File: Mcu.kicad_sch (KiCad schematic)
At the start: 11 parts, among them J2 USB C 2.0 16P, M1 Module-mega-mcu144-0.7, P23 BOOT0, P24 SWDIO, P25 SWCLK, P26 NRST, U1 USBLC6-2SC6

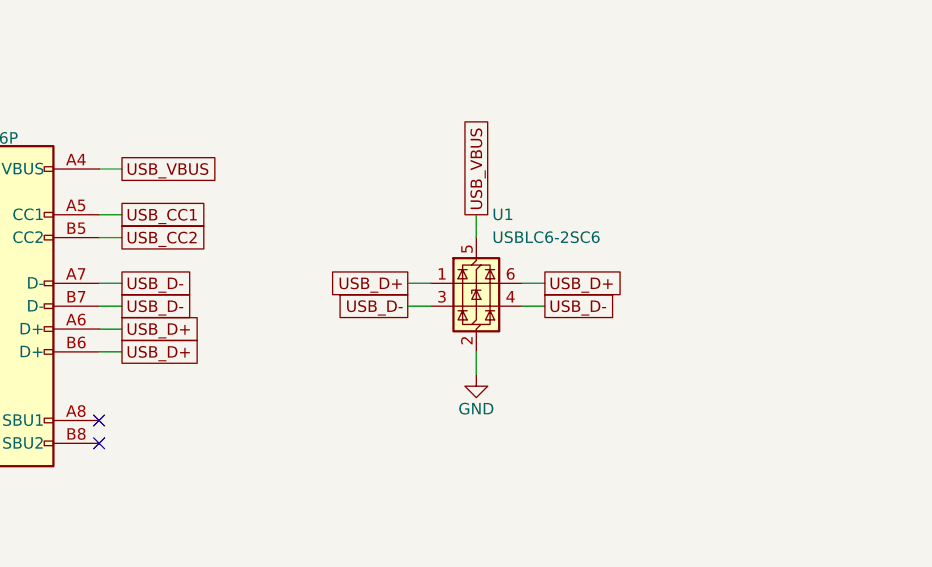
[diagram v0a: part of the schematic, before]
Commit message: U1 is the library USBLC6-2SC6 (EE-C-0146); J2 part numbers; test pads and proto area out of the BOM
- U1 used the USBLC6-2P6 (SOT-666) symbol with a hand-changed footprint; now EmbeddedEra:USBLC6-2SC6.
- J2 instance had no Manufacturer/MPN although the library has them.
- P1-P32 and G1 are pads, nothing is bought (SOP-008 step 18): in_bom no, as in the library.

Co-Authored-By: Claude Opus 5.5 <noreply@anthropic.com>
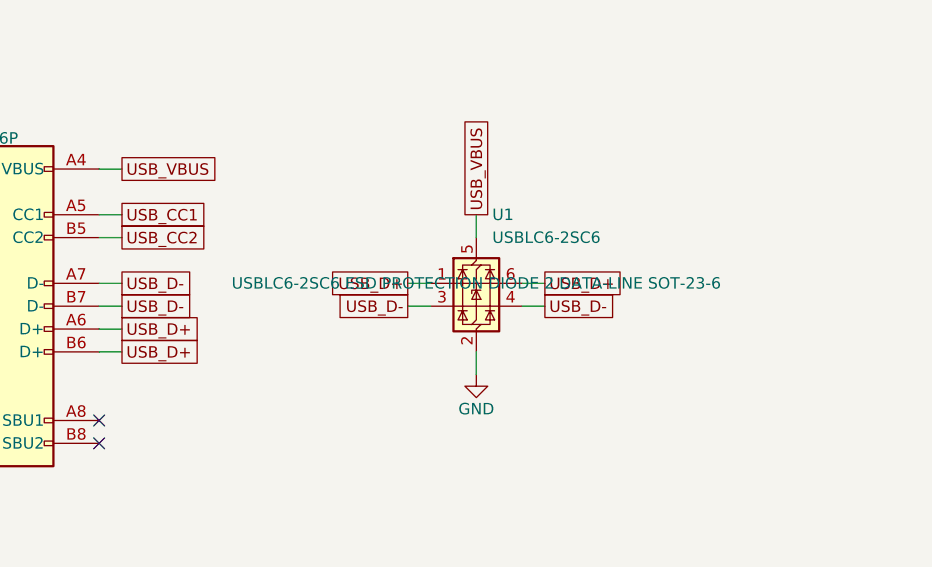
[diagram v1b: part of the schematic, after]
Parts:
- P23, P24, P25, P26: now left out of the parts list
- U1: symbol EmbeddedEra:USBLC6-2P6 -> EmbeddedEra:USBLC6-2SC6
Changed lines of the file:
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@@
 		(body_style 1)
 		(exclude_from_sim no)
-		(in_bom yes)
+		(in_bom no)
 		(on_board yes)
 		(in_pos_files yes)
@@
 		(body_style 1)
 		(exclude_from_sim no)
-		(in_bom yes)
+		(in_bom no)
 		(on_board yes)
 		(in_pos_files yes)
@@
 		(body_style 1)
 		(exclude_from_sim no)
-		(in_bom yes)
+		(in_bom no)
 		(on_board yes)
 		(in_pos_files yes)
@@
 		(body_style 1)
 		(exclude_from_sim no)
-		(in_bom yes)
+		(in_bom no)
 		(on_board yes)
 		(in_pos_files yes)
@@
 	)
 	(symbol
-		(lib_id "EmbeddedEra:USBLC6-2P6")
+		(lib_id "EmbeddedEra:USBLC6-2SC6")
 		(at 220.98 60.96 0)
 		(unit 1)
@@
 			)
 		)
-		(property "Datasheet" ""
+		(property "Datasheet" "https://www.st.com/resource/en/datasheet/usblc6-2.pdf"
 			(at 220.98 60.96 0)
 			(hide yes)
@@
 			)
 		)
-		(property "Description" ""
+		(property "Description" "USBLC6-2SC6 ESD PROTECTION DIODE 2 DATA-LINE SOT-23-6"
 			(at 220.98 60.96 0)
 			(show_name no)

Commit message: Title block: TITLE is the project name (${Project_Name}) on every sheet, DESCRIPTION the sheet name
The LS/INJ sub-sheet and the root had no title at all.

Co-Authored-By: Claude Opus 5.5 <noreply@anthropic.com>
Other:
- title: MCU and USB -> ${Project_Name}
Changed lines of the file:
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@@
 	(paper "A3" portrait)
 	(title_block
-		(title "MCU and USB")
+		(title "${Project_Name}")
 		(date "2026-10-13")
 	)

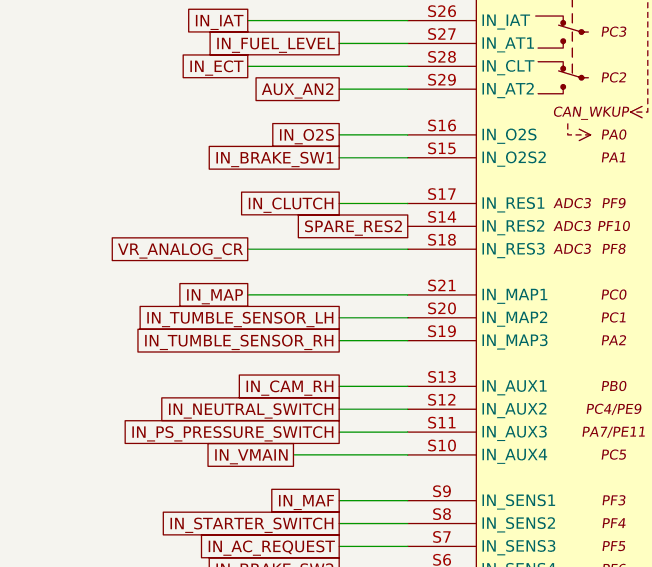
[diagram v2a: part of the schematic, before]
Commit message: On-board MAP sensor (AlphaX style): U20 MPXHZ6400AC6T1 + C1 100n on +5VA -> M1 IN_MAP3 (S19)
TGV position RH moves from IN_MAP3 to IN_RES2 (S14). J3 pin 8 (was AUX_AN1 on
IN_RES2) is now not connected; P28 is the MAP test pad. External MAP stays on
IN_MAP1. PCB: U20/C1 placed left of M1, DRC 0 errors, unconnected 322.

Co-Authored-By: Claude Opus 5.5 <noreply@anthropic.com>
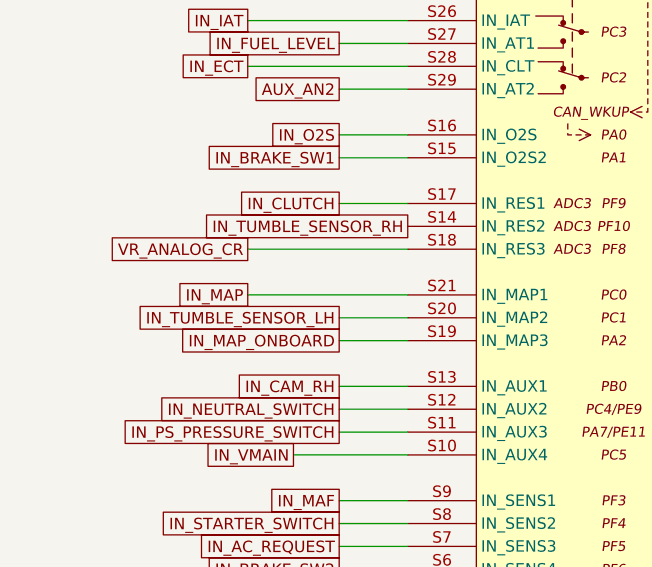
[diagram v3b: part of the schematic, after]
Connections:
- net SPARE_RES2 is gone; now on net IN_TUMBLE_SENSOR_RH: M1.S14 (IN_RES2)
- net IN_TUMBLE_SENSOR_RH: no longer M1.S19 (IN_MAP3)
- new net IN_MAP_ONBOARD: M1.S19 (IN_MAP3)

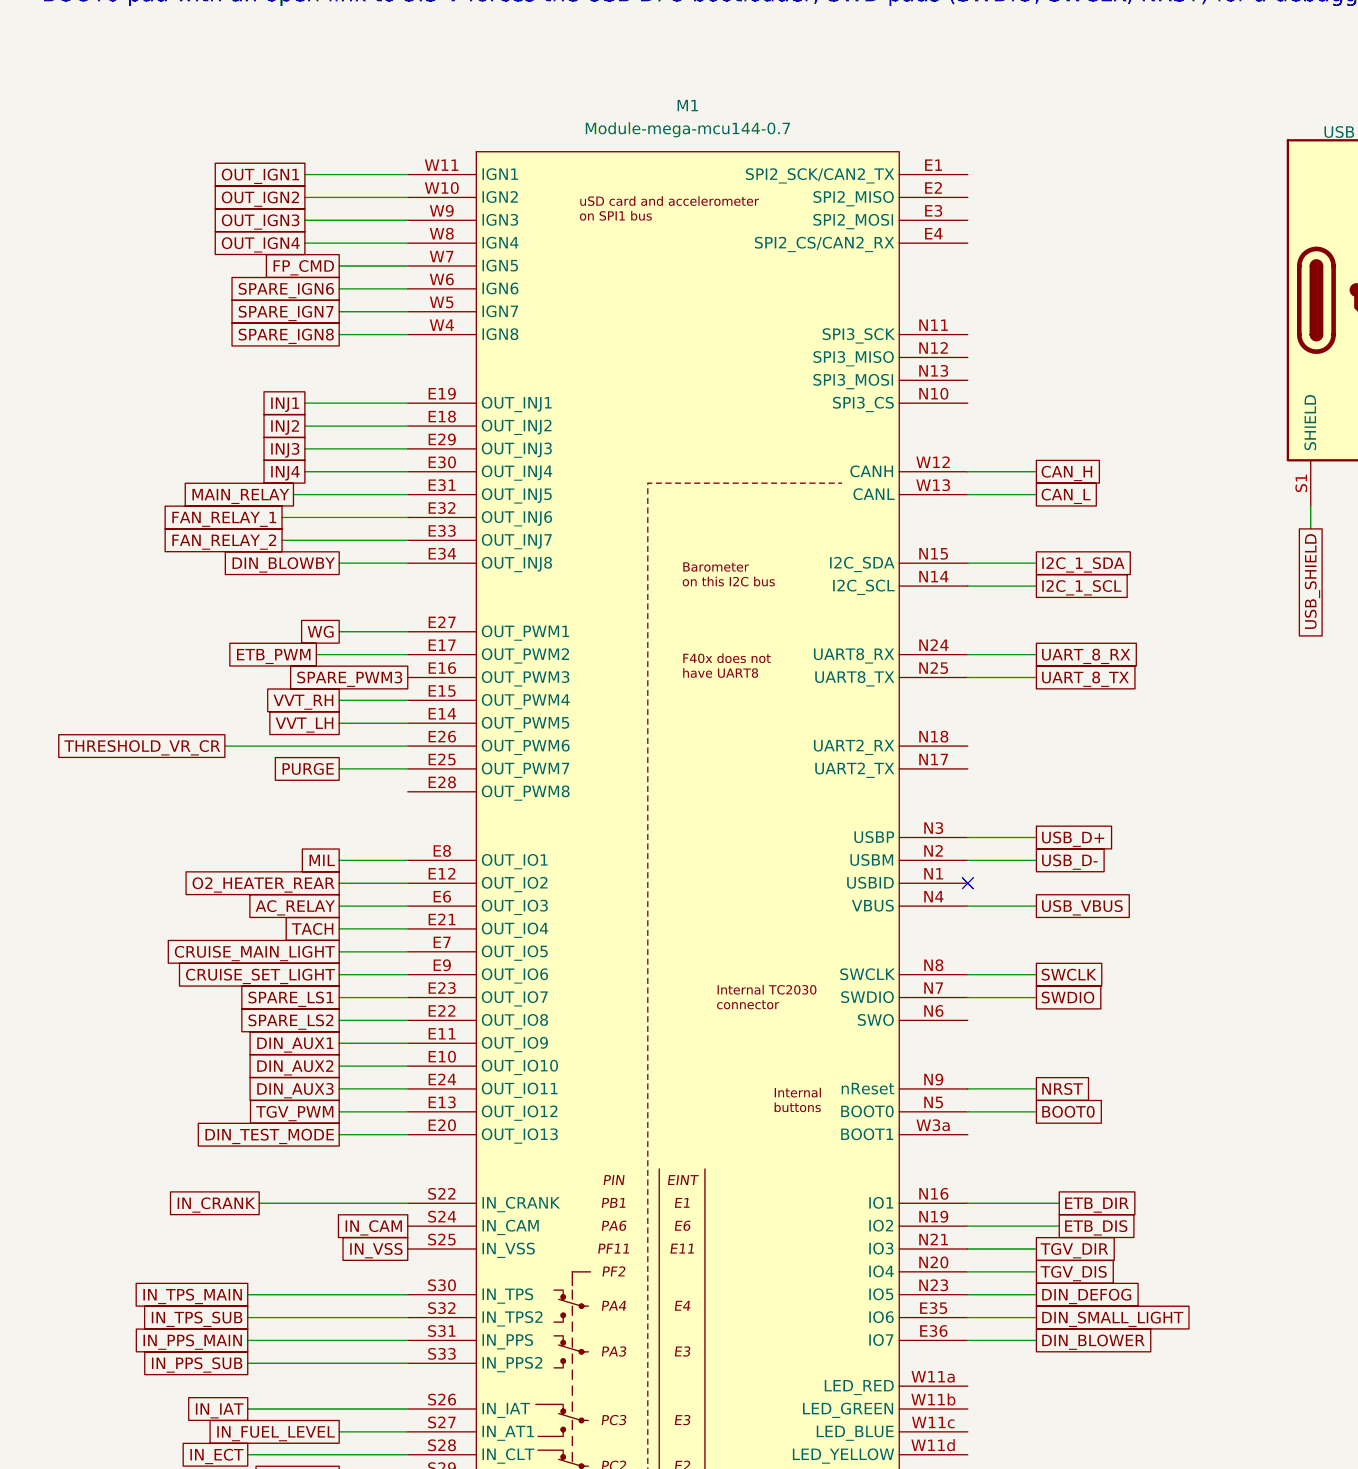
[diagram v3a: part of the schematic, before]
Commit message: M1 pin swap within module pin families (owner-approved); moved nets' copper ripped for re-routing
Co-Authored-By: Claude Opus 5.5 <noreply@anthropic.com>
Claude-Session: https://claude.ai/code/session_01Wvm7Ln3a66CJUfUkcDdYMo
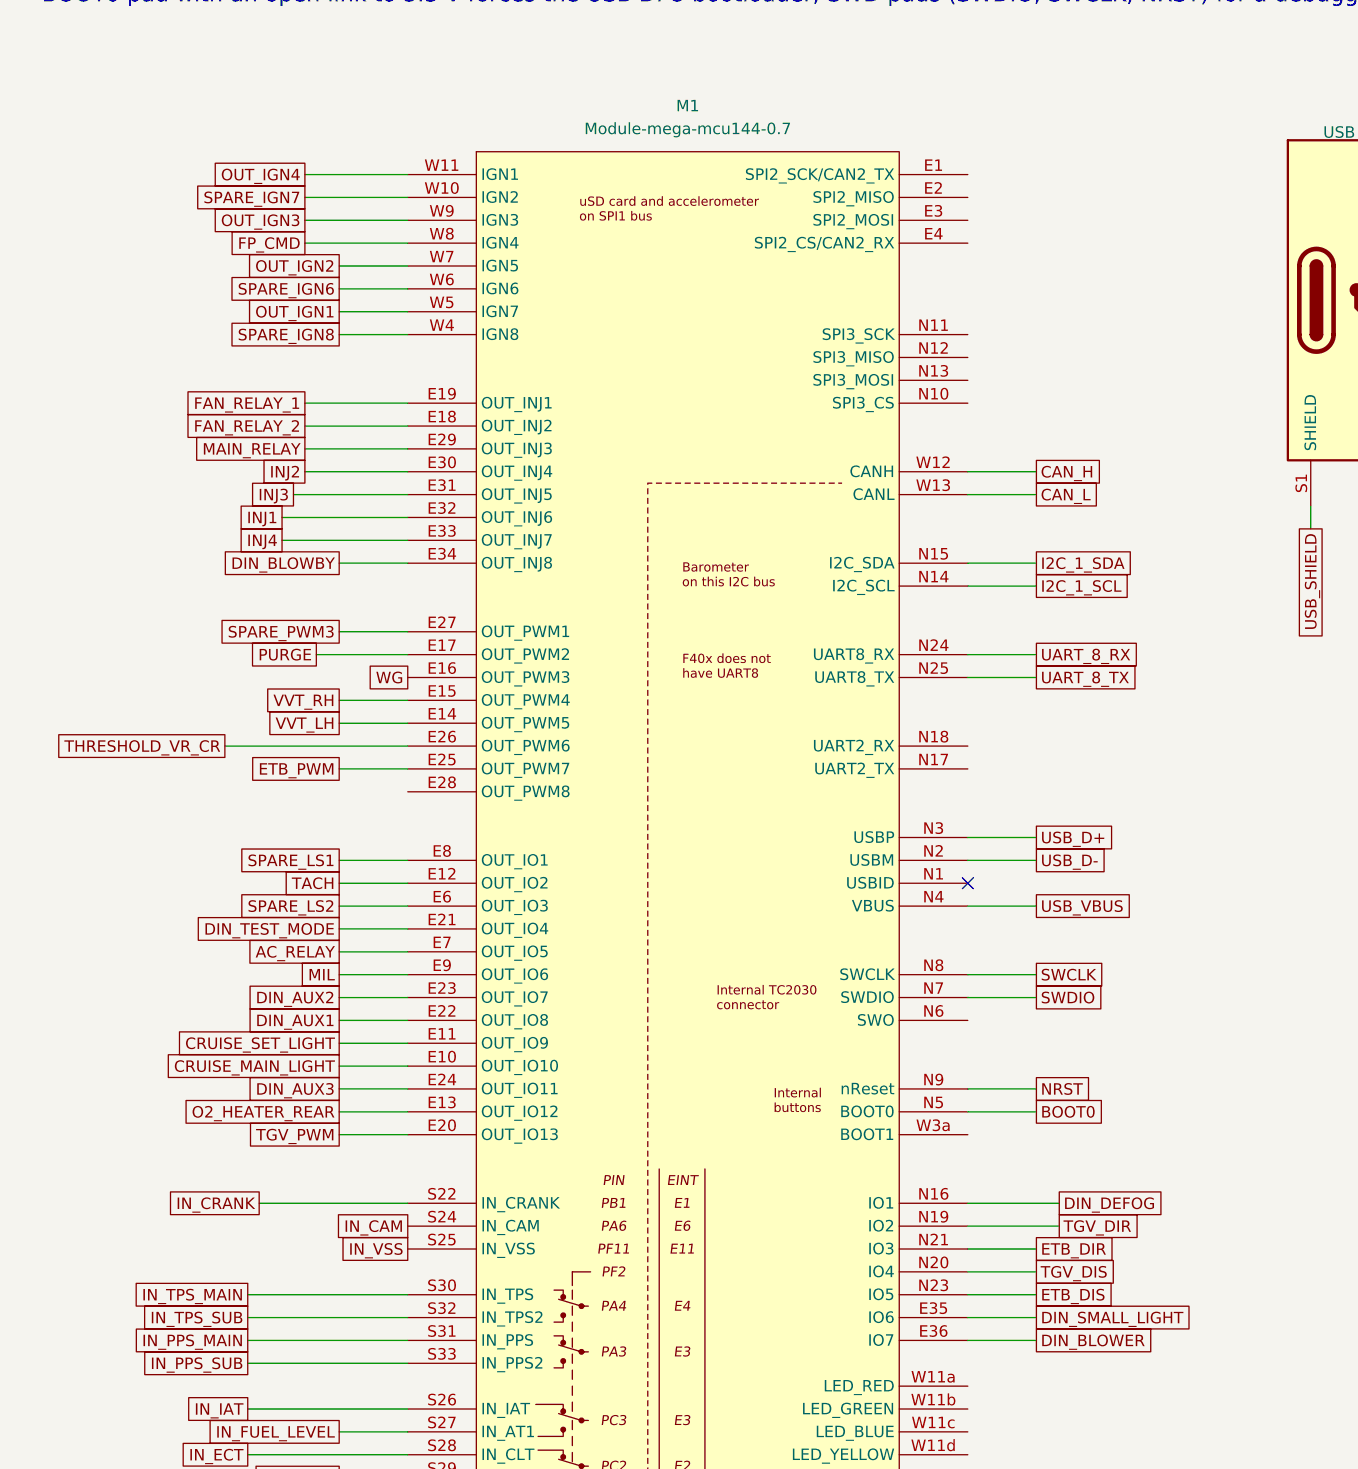
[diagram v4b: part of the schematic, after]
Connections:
- net AC_RELAY: now also M1.E7 (OUT_IO5); no longer M1.E6 (OUT_IO3)
- net CRUISE_MAIN_LIGHT: now also M1.E10 (OUT_IO10); no longer M1.E7 (OUT_IO5)
- net CRUISE_SET_LIGHT: now also M1.E11 (OUT_IO9); no longer M1.E9 (OUT_IO6)
- net DIN_AUX1: now also M1.E22 (OUT_IO8); no longer M1.E11 (OUT_IO9)
- net DIN_AUX2: now also M1.E23 (OUT_IO7); no longer M1.E10 (OUT_IO10)
- net DIN_DEFOG: now also M1.N16 (IO1); no longer M1.N23 (IO5)
- net DIN_TEST_MODE: now also M1.E21 (OUT_IO4); no longer M1.E20 (OUT_IO13)
- net ETB_DIR: now also M1.N21 (IO3); no longer M1.N16 (IO1)
- net ETB_DIS: now also M1.N23 (IO5); no longer M1.N19 (IO2)
- net ETB_PWM: now also M1.E25 (OUT_PWM7); no longer M1.E17 (OUT_PWM2)
- net FAN_RELAY_1: now also M1.E19 (OUT_INJ1); no longer M1.E32 (OUT_INJ6)
- net FAN_RELAY_2: now also M1.E18 (OUT_INJ2); no longer M1.E33 (OUT_INJ7)
- net FP_CMD: now also M1.W8 (IGN4); no longer M1.W7 (IGN5)
- net INJ1: now also M1.E32 (OUT_INJ6); no longer M1.E19 (OUT_INJ1)
- net INJ2: now also M1.E30 (OUT_INJ4); no longer M1.E18 (OUT_INJ2)
- net INJ3: now also M1.E31 (OUT_INJ5); no longer M1.E29 (OUT_INJ3)
- net INJ4: now also M1.E33 (OUT_INJ7); no longer M1.E30 (OUT_INJ4)
- net MAIN_RELAY: now also M1.E29 (OUT_INJ3); no longer M1.E31 (OUT_INJ5)
- net MIL: now also M1.E9 (OUT_IO6); no longer M1.E8 (OUT_IO1)
- net O2_HEATER_REAR: now also M1.E13 (OUT_IO12); no longer M1.E12 (OUT_IO2)
- net OUT_IGN1: now also M1.W5 (IGN7); no longer M1.W11 (IGN1)
- net OUT_IGN2: now also M1.W7 (IGN5); no longer M1.W10 (IGN2)
- net OUT_IGN4: now also M1.W11 (IGN1); no longer M1.W8 (IGN4)
- net PURGE: now also M1.E17 (OUT_PWM2); no longer M1.E25 (OUT_PWM7)
- net SPARE_IGN7: now also M1.W10 (IGN2); no longer M1.W5 (IGN7)
- net SPARE_LS1: now also M1.E8 (OUT_IO1); no longer M1.E23 (OUT_IO7)
- net SPARE_LS2: now also M1.E6 (OUT_IO3); no longer M1.E22 (OUT_IO8)
- net SPARE_PWM3: now also M1.E27 (OUT_PWM1); no longer M1.E16 (OUT_PWM3)
- net TACH: now also M1.E12 (OUT_IO2); no longer M1.E21 (OUT_IO4)
- net TGV_DIR: now also M1.N19 (IO2); no longer M1.N21 (IO3)
- net TGV_PWM: now also M1.E20 (OUT_IO13); no longer M1.E13 (OUT_IO12)
- net WG: now also M1.E16 (OUT_PWM3); no longer M1.E27 (OUT_PWM1)
